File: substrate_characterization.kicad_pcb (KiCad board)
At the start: 4 copper layers, 62.5 x 106.9 mm, 14 parts, among them J1 5.8G-P1, J10 L2-P2, J11 L1F-P2, J12 L2F-P2, J2 2.9G-P1, J3 L1-P1, J4 L2-P1, J5 L1F-P1, J6 L2F-P1, J7 5.8G-P2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

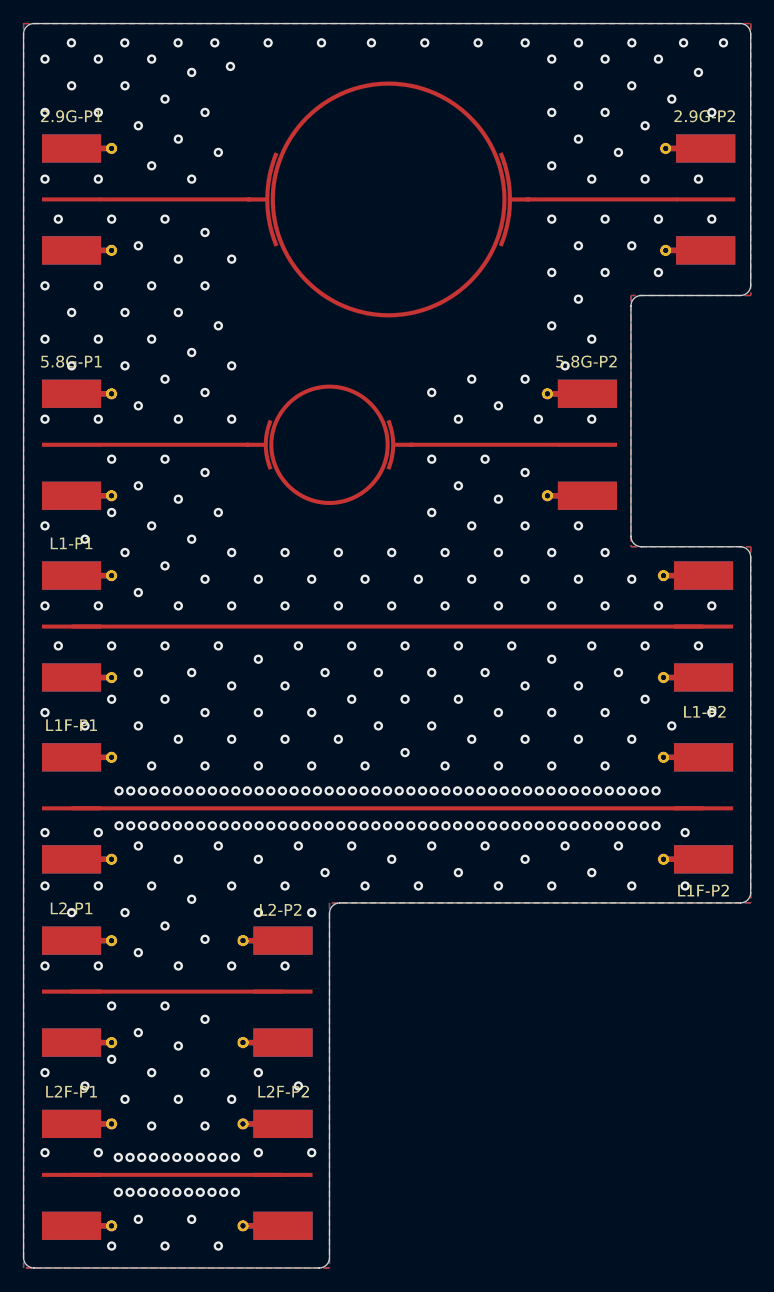
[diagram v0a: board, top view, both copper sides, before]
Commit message: Footprint updates for sma
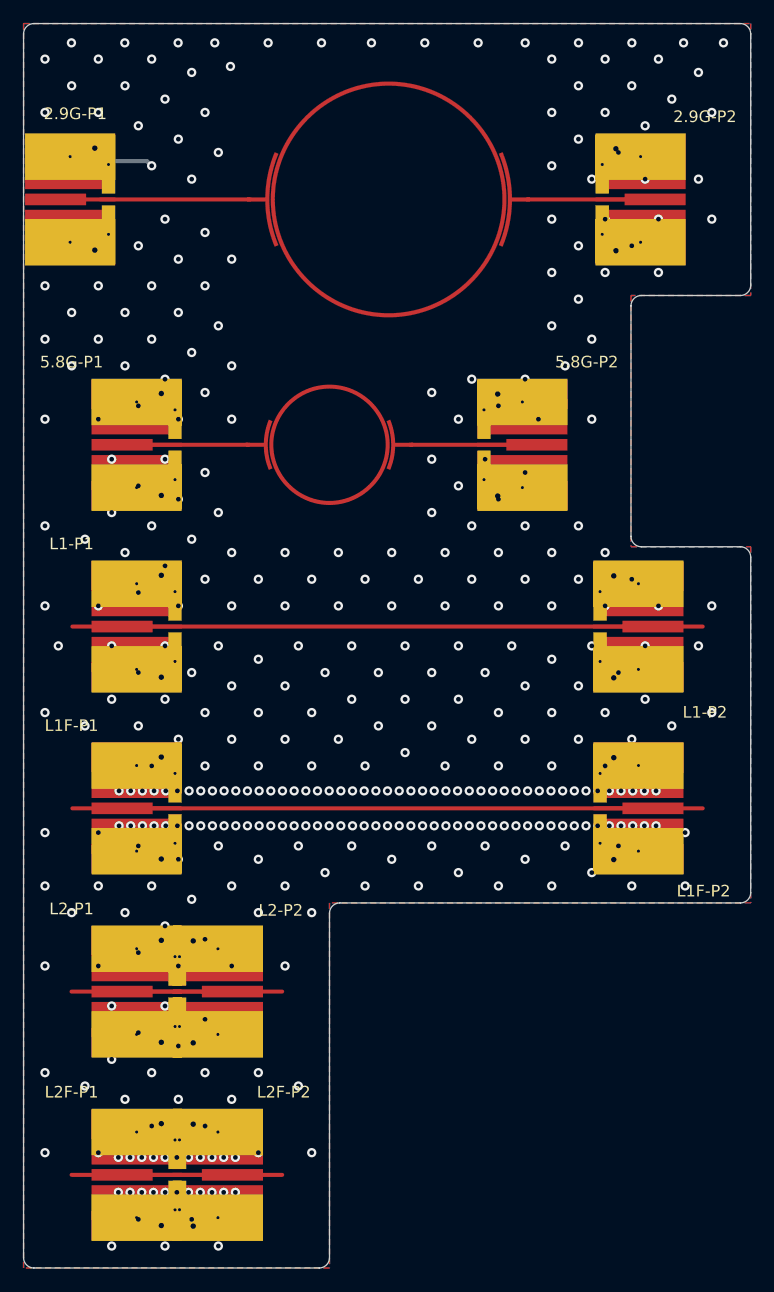
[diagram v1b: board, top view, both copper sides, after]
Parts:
- J1, J10, J11, J12, J2, J3, J4, J5, J6, J7, J8, J9: footprint aps_radar_lib:SMA_Molex_73251-1153_EdgeMount_Horizontal -> aps_radar_lib:SMA_Molex_Transition
- moved J2 5.71 mm to (63.4, 53.3)
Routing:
- net GND: track 0.00 -> 4.09 mm, vias 397 -> 393
